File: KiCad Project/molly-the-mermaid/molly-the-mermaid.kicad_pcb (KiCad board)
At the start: 2 copper layers, 61 x 81.1 mm, 41 parts, among them J1 SAO, SW1 Left, SW2 Up, SW3 Right, SW4 Down, SW5 B, SW6 A, U1 SC0915

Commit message: connected grounds
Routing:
- net GND: track 0.00 -> 2.42 mm, vias 4 -> 9
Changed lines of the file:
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@@
   (arc (start 208.964214 108.126214) (mid 209.61306 108.559759) (end 210.378427 108.712) (width 0.508) (layer "B.Cu") (net 1))
   (via (at 237.236 82.042) (size 0.8) (drill 0.4) (layers "F.Cu" "B.Cu") (free) (net 2))
+  (via (at 220.726 99.06) (size 0.8) (drill 0.4) (layers "F.Cu" "B.Cu") (free) (net 2))
+  (via (at 220.218 108.204) (size 0.8) (drill 0.4) (layers "F.Cu" "B.Cu") (free) (net 2))
+  (via (at 205.486 100.584) (size 0.8) (drill 0.4) (layers "F.Cu" "B.Cu") (free) (net 2))
   (via (at 226.822 84.328) (size 0.8) (drill 0.4) (layers "F.Cu" "B.Cu") (free) (net 2))
   (via (at 195.834 126.238) (size 0.8) (drill 0.4) (layers "F.Cu" "B.Cu") (free) (net 2))
   (via (at 206.502 82.042) (size 0.8) (drill 0.4) (layers "F.Cu" "B.Cu") (free) (net 2))
+  (via (at 199.898 94.234) (size 0.8) (drill 0.4) (layers "F.Cu" "B.Cu") (free) (net 2))
+  (via (at 211.836 95.504) (size 0.8) (drill 0.4) (layers "F.Cu" "B.Cu") (free) (net 2))
+  (segment (start 220.726 99.06) (end 220.726 100.35286) (width 0.254) (layer "B.Cu") (net 2))
+  (segment (start 220.726 100.35286) (end 219.9259 101.15296) (width 0.254) (layer "B.Cu") (net 2))
   (segment (start 211.241787 81.344713) (end 211.8145 80.772) (width 0.3048) (layer "F.Cu") (net 3))
   (segment (start 241.644 120.574) (end 241.644 119.842927) (width 0.3048) (layer "F.Cu") (net 3))

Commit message: another missing ground
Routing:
- net GND: vias 9 -> 10
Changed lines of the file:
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@@
   (via (at 226.822 84.328) (size 0.8) (drill 0.4) (layers "F.Cu" "B.Cu") (free) (net 2))
   (via (at 195.834 126.238) (size 0.8) (drill 0.4) (layers "F.Cu" "B.Cu") (free) (net 2))
+  (via (at 209.042 118.872) (size 0.8) (drill 0.4) (layers "F.Cu" "B.Cu") (free) (net 2))
   (via (at 206.502 82.042) (size 0.8) (drill 0.4) (layers "F.Cu" "B.Cu") (free) (net 2))
   (via (at 199.898 94.234) (size 0.8) (drill 0.4) (layers "F.Cu" "B.Cu") (free) (net 2))

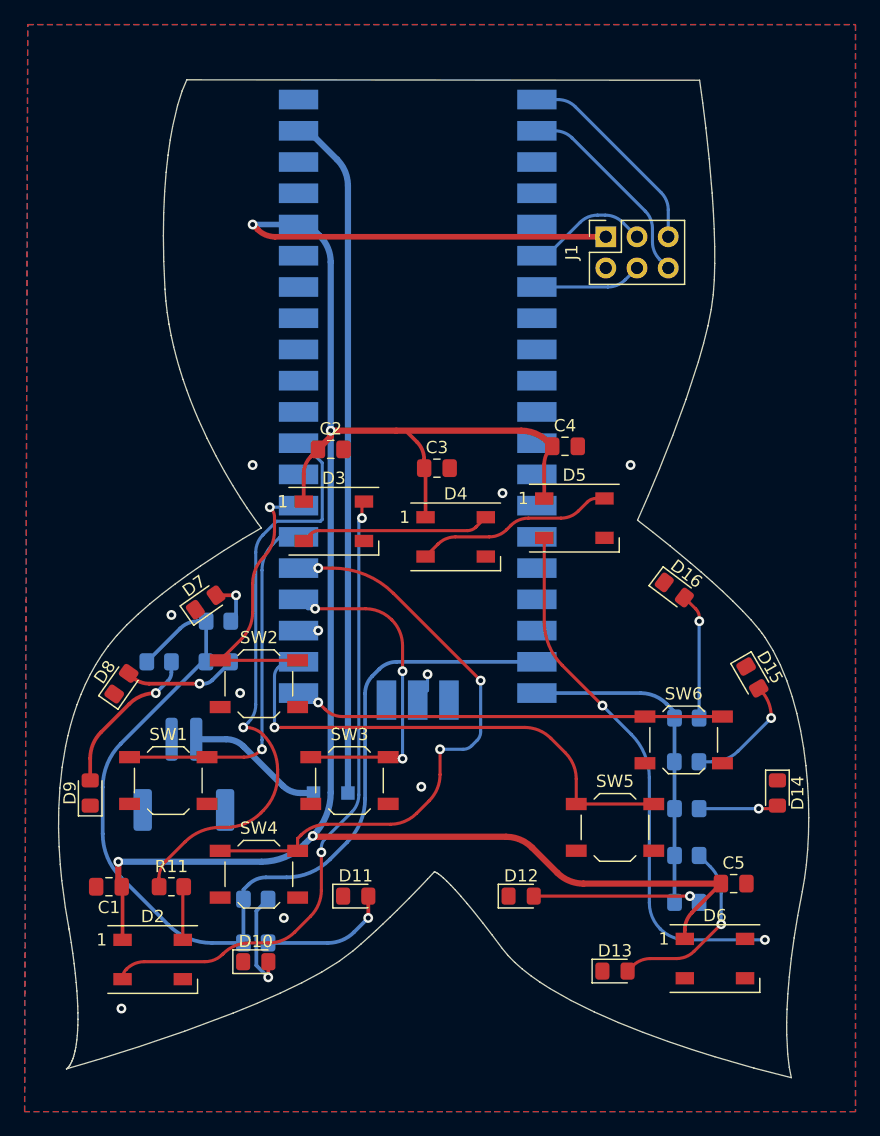
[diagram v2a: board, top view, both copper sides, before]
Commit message: cleared some DRC errors
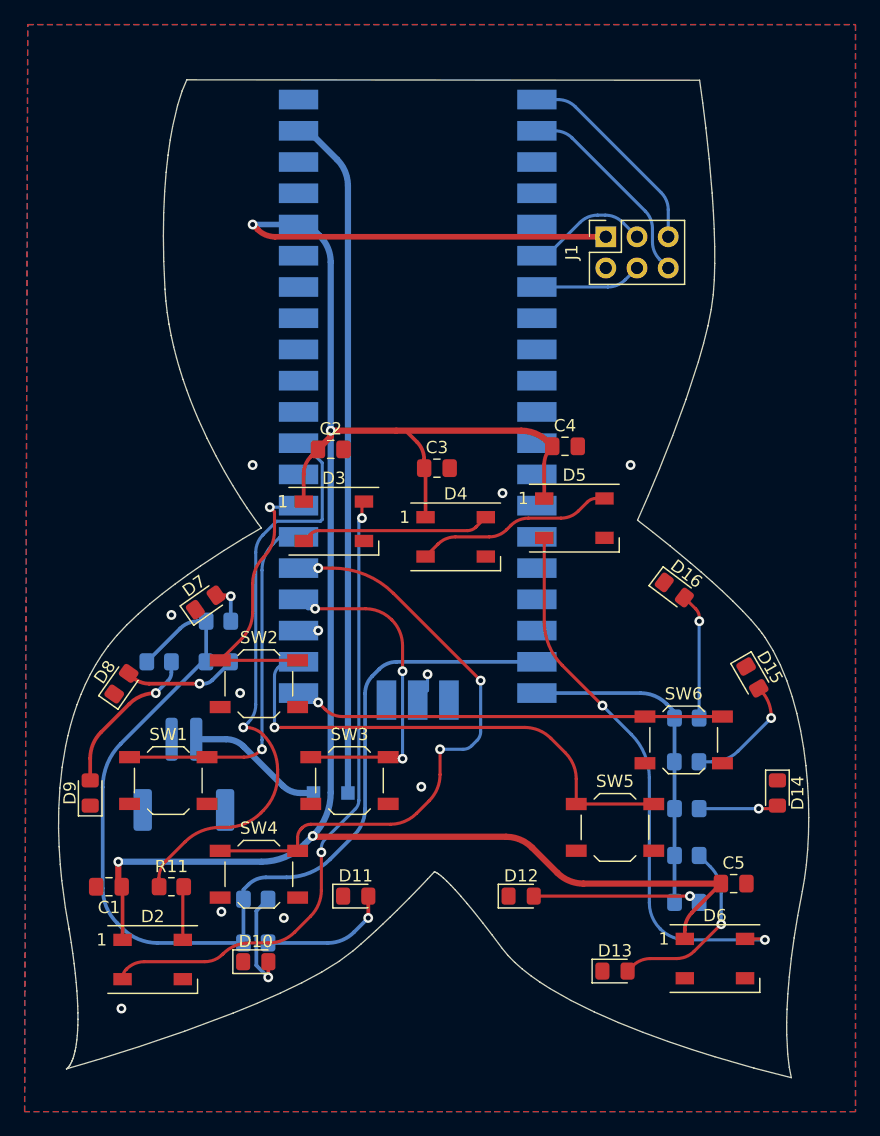
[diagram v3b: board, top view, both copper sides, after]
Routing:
- net Net-(R1-Pad2): track 84.5 -> 87.0 mm
- net Net-(D5-Pad2): track 43.8 -> 45.5 mm
- net Net-(D7-Pad2): track 4.03 -> 3.27 mm
- net GND: vias 10 -> 11

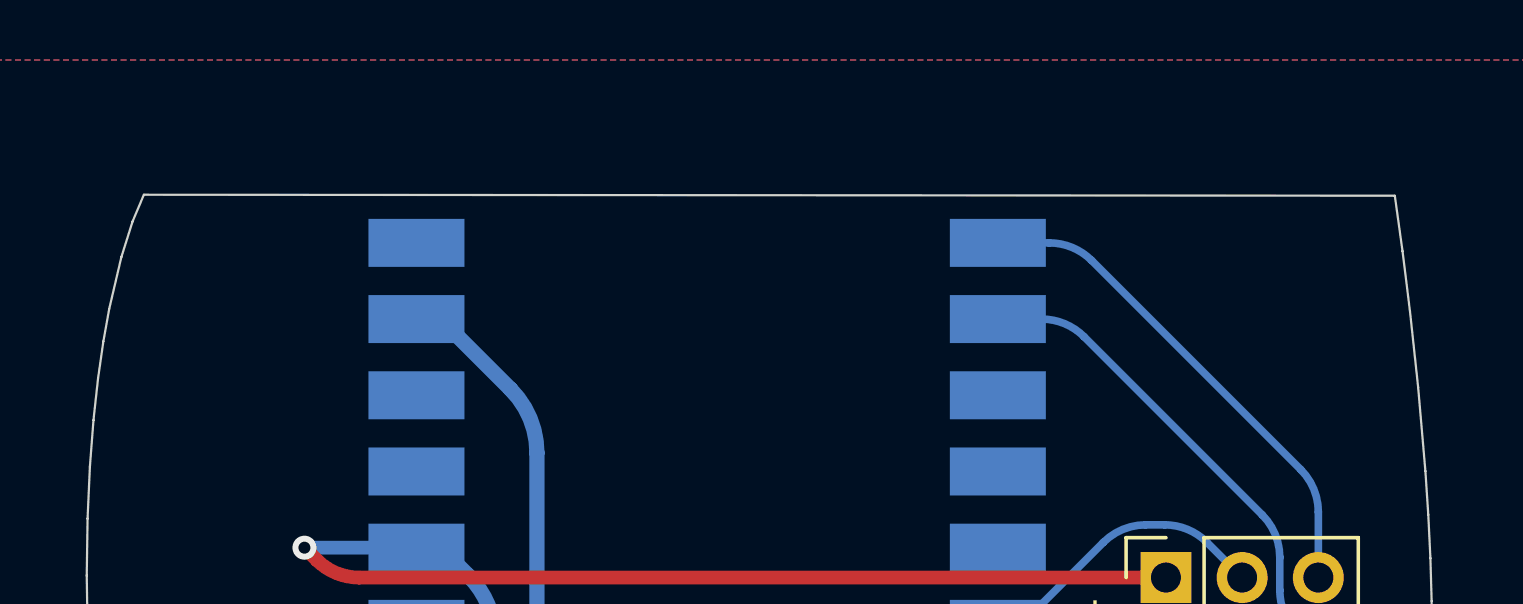
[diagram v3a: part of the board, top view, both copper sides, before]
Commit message: add mounting holes
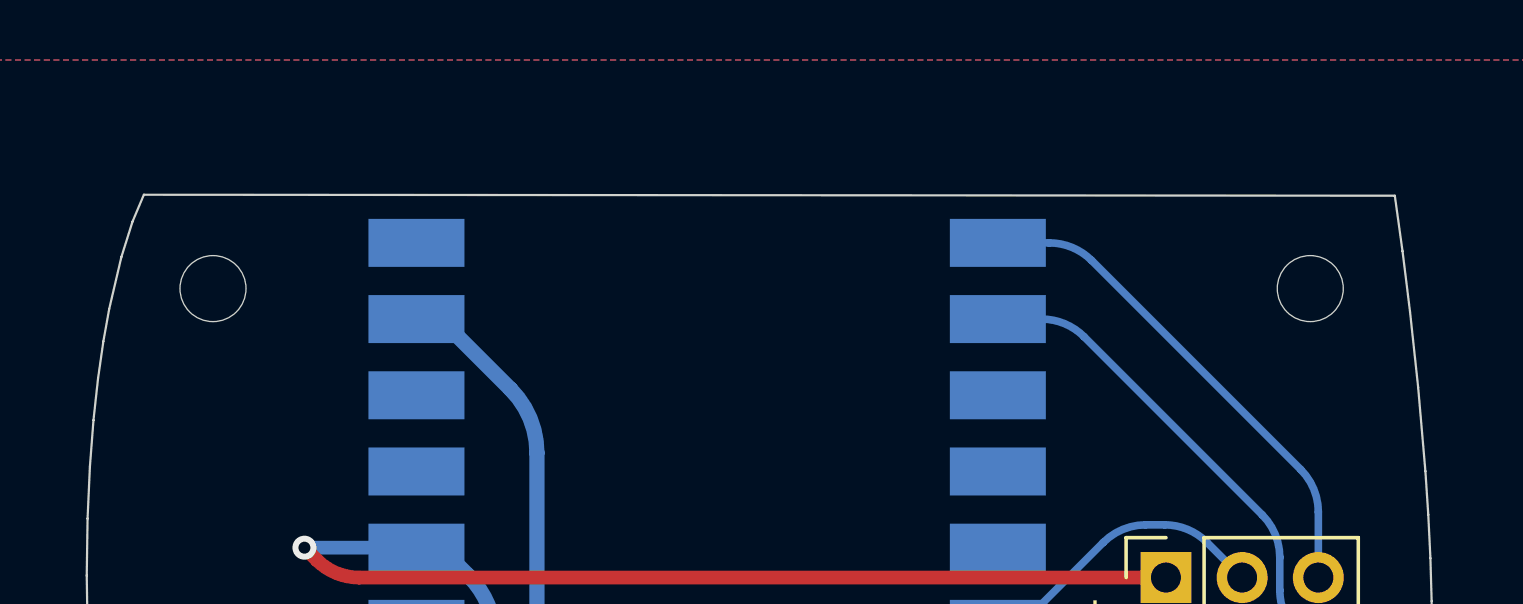
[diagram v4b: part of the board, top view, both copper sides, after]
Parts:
- added H1: MountingHole, MountingHole:MountingHole_2.2mm_M2, F.Cu at (203.5, 53.8)
- added H2: MountingHole, MountingHole:MountingHole_2.2mm_M2, F.Cu at (240.0, 53.8)
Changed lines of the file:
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@@
     )
+  )
+  (footprint "MountingHole:MountingHole_2.2mm_M2" (layer "F.Cu")
+    (at 203.454 53.848)
+    (descr "Mounting Hole 2.2mm, no annular, M2")
+    (tags "mounting hole 2.2mm no annular m2")
+    (property "Sheetfile" "molly-the-mermaid.kicad_sch")
+    (property "Sheetname" "")
+    (attr exclude_from_pos_files)
+    (fp_text reference "H1" (at 0 -3.2) (layer "F.SilkS") hide
+      (effects (font (size 1 1) (thickness 0.15)))
+    )
+    (fp_text value "MountingHole" (at 0 3.2) (layer "F.Fab")
+      (effects (font (size 1 1) (thickness 0.15)))
+    )
+    (fp_text user "${REFERENCE}" (at 0.3 0) (layer "F.Fab")
+      (effects (font (size 1 1) (thickness 0.15)))
+    )
+    (fp_circle (center 0 0) (end 2.2 0) (layer "Cmts.User") (width 0.15) (fill none))
+    (fp_circle (center 0 0) (end 2.45 0) (layer "F.CrtYd") (width 0.05) (fill none))
+    (pad "" np_thru_hole circle locked (at 0 0) (size 2.2 2.2) (drill 2.2) (layers *.Cu *.Mask))
+  )
+  (footprint "MountingHole:MountingHole_2.2mm_M2" (layer "F.Cu")
+    (at 240.03 53.848)
+    (descr "Mounting Hole 2.2mm, no annular, M2")
+    (tags "mounting hole 2.2mm no annular m2")
+    (property "Sheetfile" "molly-the-mermaid.kicad_sch")
+    (property "Sheetname" "")
+    (attr exclude_from_pos_files)
+    (fp_text reference "H2" (at 0 -3.2) (layer "F.SilkS") hide
+      (effects (font (size 1 1) (thickness 0.15)))
+    )
+    (fp_text value "MountingHole" (at 0 3.2) (layer "F.Fab")
+      (effects (font (size 1 1) (thickness 0.15)))
+    )
+    (fp_text user "${REFERENCE}" (at 0.3 0) (layer "F.Fab")
+      (effects (font (size 1 1) (thickness 0.15)))
+    )
+    (fp_circle (center 0 0) (end 2.2 0) (layer "Cmts.User") (width 0.15) (fill none))
+    (fp_circle (center 0 0) (end 2.45 0) (layer "F.CrtYd") (width 0.05) (fill none))
+    (pad "" np_thru_hole circle locked (at 0 0) (size 2.2 2.2) (drill 2.2) (layers *.Cu *.Mask))
   )
   (footprint "LED_SMD:LED_WS2812B_PLCC4_5.0x5.0mm_P3.2mm" (layer "F.Cu")

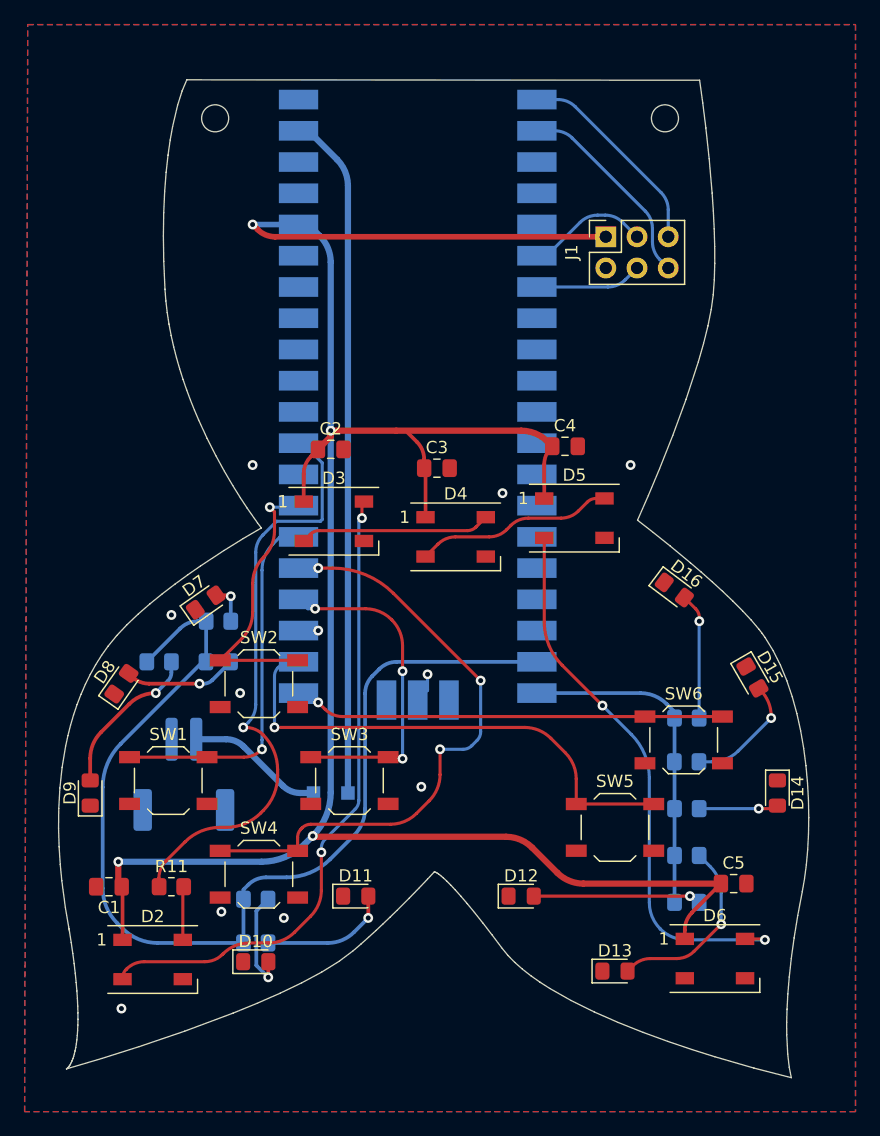
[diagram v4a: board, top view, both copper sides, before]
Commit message: Added component values to schematic
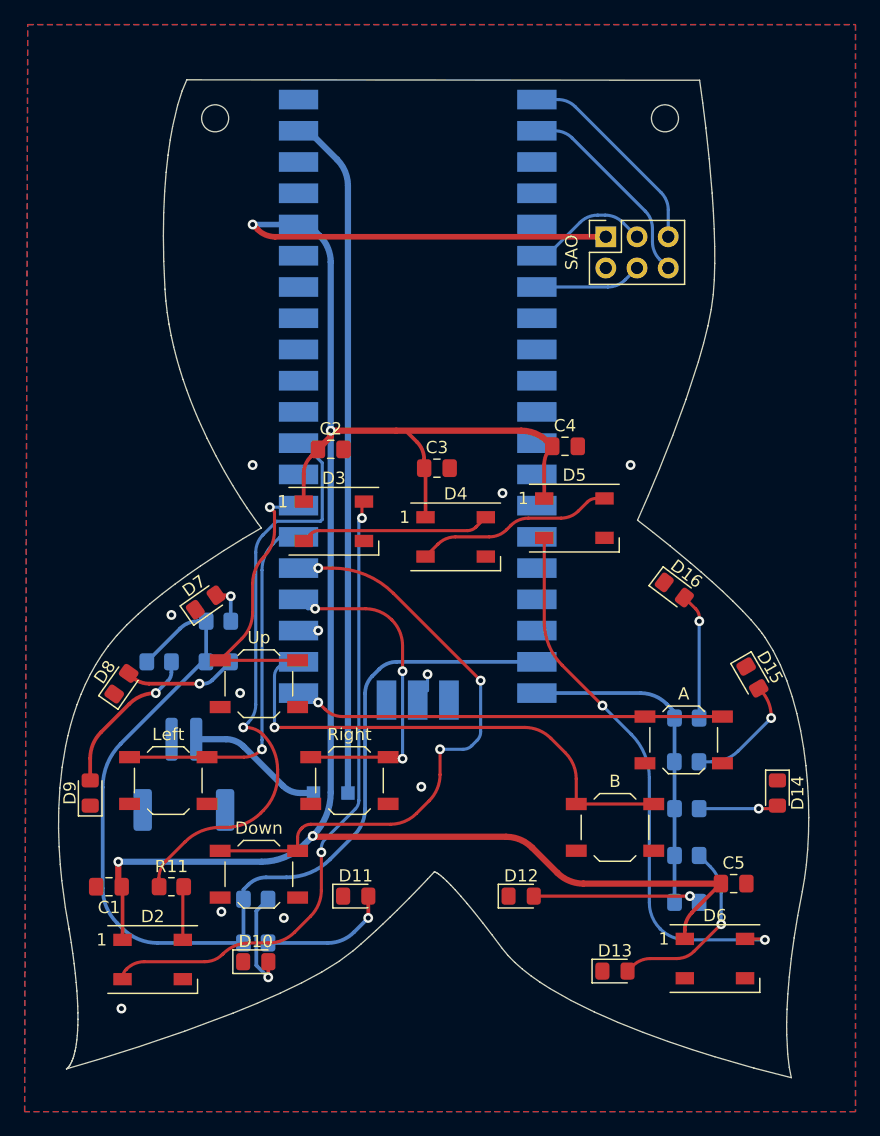
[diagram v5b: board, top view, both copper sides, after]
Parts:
- renumbered SW6 to A, SW5 to B, SW4 to Down, SW1 to Left, SW3 to Right, J1 to SAO, SW2 to Up
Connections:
- BT1 pad MP: (no net) -> GND
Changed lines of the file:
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@@
     (property "Sheetname" "")
     (attr smd)
-    (fp_text reference "SW3" (at 0 -3.75) (layer "F.SilkS")
+    (fp_text reference "Right" (at 0 -3.75) (layer "F.SilkS")
       (effects (font (size 1 1) (thickness 0.15)))
     )
@@
     (property "Sheetname" "")
     (attr smd)
-    (fp_text reference "SW4" (at 0 -3.75) (layer "F.SilkS")
+    (fp_text reference "Down" (at 0 -3.75) (layer "F.SilkS")
       (effects (font (size 1 1) (thickness 0.15)))
     )
@@
     (property "Sheetname" "")
     (attr smd)
-    (fp_text reference "SW6" (at 0 -3.75) (layer "F.SilkS")
+    (fp_text reference "A" (at 0 -3.75) (layer "F.SilkS")
       (effects (font (size 1 1) (thickness 0.15)))
     )
@@
     (property "Sheetname" "")
     (attr through_hole)
-    (fp_text reference "J1" (at -1.27 -2.77 90) (layer "F.SilkS")
+    (fp_text reference "SAO" (at -1.27 -2.77 90) (layer "F.SilkS")
       (effects (font (size 1 1) (thickness 0.15)))
     )
@@
     (property "Sheetname" "")
     (attr smd)
-    (fp_text reference "SW2" (at 0 -3.75) (layer "F.SilkS")
+    (fp_text reference "Up" (at 0 -3.75) (layer "F.SilkS")
       (effects (font (size 1 1) (thickness 0.15)))
     )
@@
     (property "Sheetname" "")
     (attr smd)
-    (fp_text reference "SW1" (at 0 -3.75) (layer "F.SilkS")
+    (fp_text reference "Left" (at 0 -3.75) (layer "F.SilkS")
       (effects (font (size 1 1) (thickness 0.15)))
     )
@@
     (property "Sheetname" "")
     (attr smd)
-    (fp_text reference "SW5" (at 0 -3.75) (layer "F.SilkS")
+    (fp_text reference "B" (at 0 -3.75) (layer "F.SilkS")
       (effects (font (size 1 1) (thickness 0.15)))
     )
@@
     (pad "2" smd roundrect locked (at 1 2.85 180) (size 1 3.5) (layers "B.Cu" "B.Paste" "B.Mask") (roundrect_rratio 0.25)
       (net 2 "GND") (pinfunction "-") (pintype "passive"))
-    (pad "MP" smd roundrect locked (at 3.35 -2.9 180) (size 1.5 3.4) (layers "B.Cu" "B.Paste" "B.Mask") (roundrect_rratio 0.1666673333))
-    (pad "MP" smd roundrect locked (at -3.35 -2.9 180) (size 1.5 3.4) (layers "B.Cu" "B.Paste" "B.Mask") (roundrect_rratio 0.1666673333))
+    (pad "MP" smd roundrect locked (at 3.35 -2.9 180) (size 1.5 3.4) (layers "B.Cu" "B.Paste" "B.Mask") (roundrect_rratio 0.1666673333)
+      (net 2 "GND") (thermal_width 1))
+    (pad "MP" smd roundrect locked (at -3.35 -2.9 180) (size 1.5 3.4) (layers "B.Cu" "B.Paste" "B.Mask") (roundrect_rratio 0.1666673333)
+      (net 2 "GND") (thermal_width 1))
     (model "${KICAD6_3DMODEL_DIR}/Connector_JST.3dshapes/JST_PH_S2B-PH-SM4-TB_1x02-1MP_P2.00mm_Horizontal.wrl"
       (offset (xyz 0 0 0))

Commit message: Board draft 2
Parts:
- U1: value SC0915 -> Raspberry Pi Pico
- renumbered BT1 to Battery
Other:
- board text added: "+"
- board text added: "GP16"
- board text added: "GP17"
- board text added: "GP18"
- board text added: "GP19"
- board text added: "GP20"
- board text added: "GP21"
- board text added: "Love is Love Trans rights are human rights!"
- board text added: "Molly the Mermaid by @GalaxyAllie and friends"

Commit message: moved SAO connector up
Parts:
- Body (SAO): renamed from SAO
- moved Body (SAO) 4.03 mm to (236.1, 59.5)
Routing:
- net +3V3: track 185.1 -> 179.2 mm
- net /SAO1: track 16.9 -> 14.2 mm
- net /SCL: track 8.69 -> 11.0 mm
- net /SAO2: track 16.6 -> 15.1 mm
- net /SDA: track 10.0 -> 11.2 mm

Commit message: Final draft board
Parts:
- SAO: renamed from Body (SAO)
- U1: value Raspberry Pi Pico -> (Pico)
